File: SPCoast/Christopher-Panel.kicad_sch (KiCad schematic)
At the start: 23 parts, among them U10028 0x27, U10029 0x28, U10030 0x29

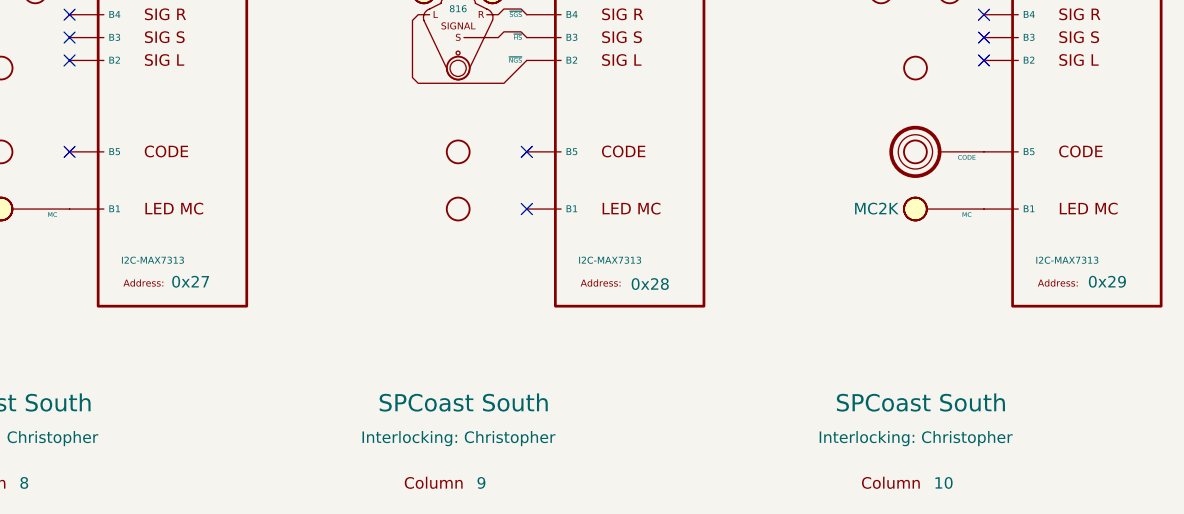
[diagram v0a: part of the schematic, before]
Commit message: chore(kicad): SPCoast symbols refreshed, field attribute visibility, no-connects on unused pins (owner's edit, baseline)
Owner, 2026-10-08: updated symbols from the libraries (the field pin direction flip, InterlockingPlant
61269e0), adjusted attribute visibility, added 22 no-connect markers on unused pins.

Verified (committed as saved, no edits):
- 485 components, 648 nets; every net identical to the previous commit.
- ERC 53 -> 20 messages (13 errors, 7 warnings). Remaining: unconnected HOUSE H / aux MC pins
  (Gilroy Caltrain, Luchessa, Watsonville); Corporal SW11901 still Railroad:Switch_HandThrow (not in
  the library) with open N/R legs; Sargent switch 1 open N/R legs; Christopher Panel U10029 A6 open
  while lamp LMP10093 carries a no-connect; 5 inherited wire stubs.
- Every instance path starts at the root uuid.

Co-Authored-By: Claude Opus 5.5 <noreply@anthropic.com>
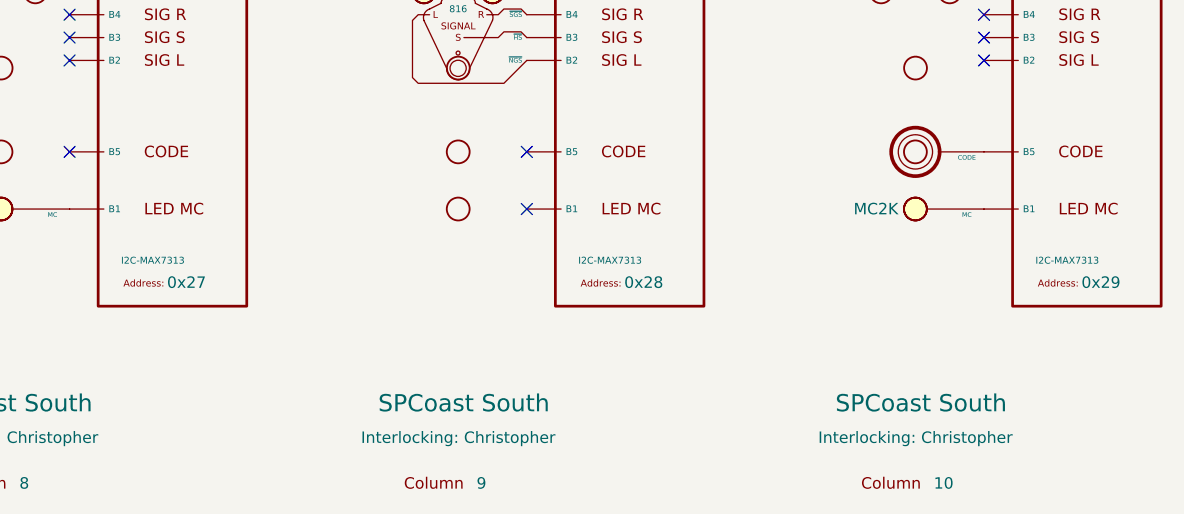
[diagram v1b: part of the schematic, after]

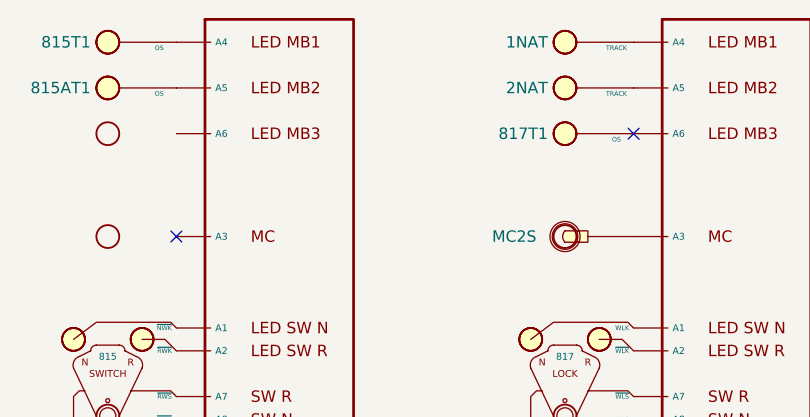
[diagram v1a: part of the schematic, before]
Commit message: fix(kicad): SPCoast ERC clean: Corporal SW11901 to Switch_Manual_Sensed, Christopher lamp fixed, no-connects (owner's edit, baseline)
Owner, 2026-10-08. Corporal and Sargent's industry tracks (the beet loader) join each other outside
CTC: dark track, no routes, no NextCP.

Verified (committed as saved, no edits): 485 components, 648 nets; ERC 0 errors, 0 warnings.

Co-Authored-By: Claude Opus 5.5 <noreply@anthropic.com>
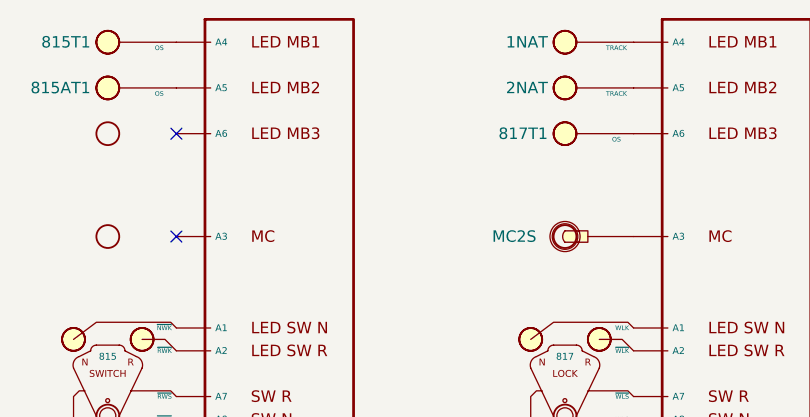
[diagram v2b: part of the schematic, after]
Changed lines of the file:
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@@
+	)
+	(no_connect
+		(at 138.43 36.83)
 	)
 	(no_connect
@@
 	)
 	(no_connect
-		(at 189.23 36.83)
-	)
-	(no_connect

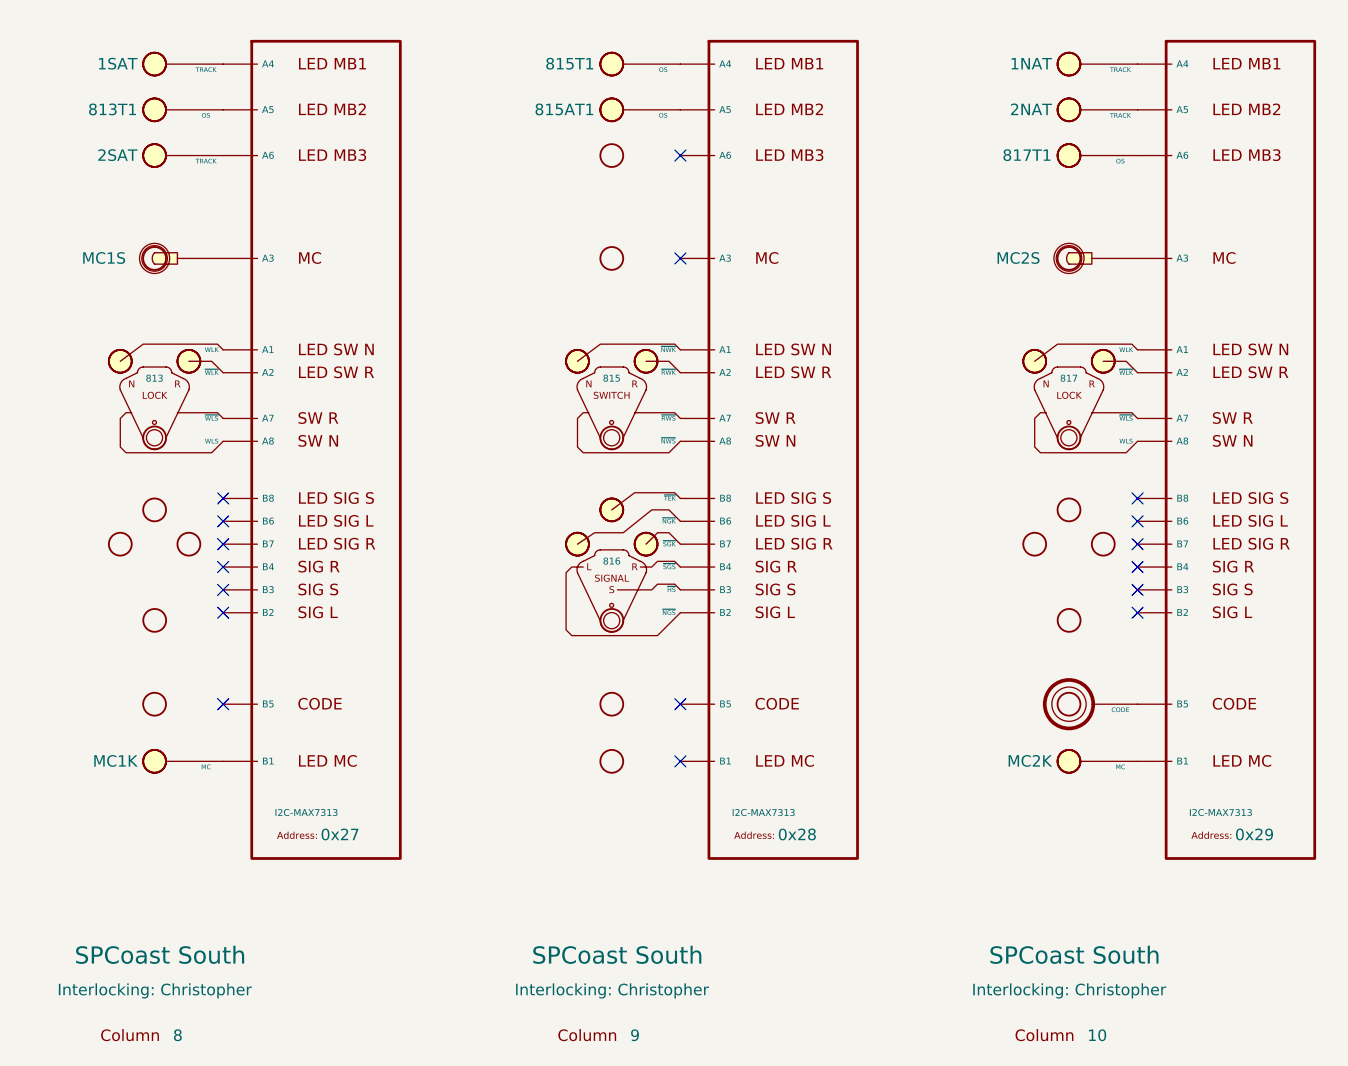
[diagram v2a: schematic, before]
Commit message: feat(spcoast): every sheet on the four Railroad libraries (checkpoint step 6, mechanical half)
By SPCoast/edits/2026-10-12-migrate-libraries.py, run once with KiCad closed: 483 instances
remapped across 16 sheets, embedded definitions replaced by the library blocks, instance fields
synced (Kind, ControlToken, Vital, NormalIs, Chain, Index dropped; Indications renamed
IndicationCeiling; Hold_ms renamed hold_ms; a pixel's Index became its Address; Rulebook kept
on the four Luchessa markers because the compiler still reads it), and 22 units added at the
same position for the plates and devices that are multi-unit now. Owner's choices: every plant
head CPL; Sargent's semaphore UQ; the 0x27 PCA9685 as PWM; the office MAX7313s as the
SPCoastcTc variant. Left by hand: the two AUXILIARY_TRAFFIC markers on Watsonville (retired).

Verified (production/migration-gate.txt, netlist_diff.py against pre-migration.net): office
and local plates and all chips keep their connectivity; 14 nets lost, all on Sargent, where
the six field devices (DevSW13001, 13004 to 13007, 13012) have new pin positions and must be
re-wired by hand. ERC: lib_symbol_issues 492 before (unregistered libraries) to 2 after (the
retired markers); the 29 unconnected pins are those devices and their chip pins.

Co-Authored-By: Claude Fable 5.1 <noreply@anthropic.com>
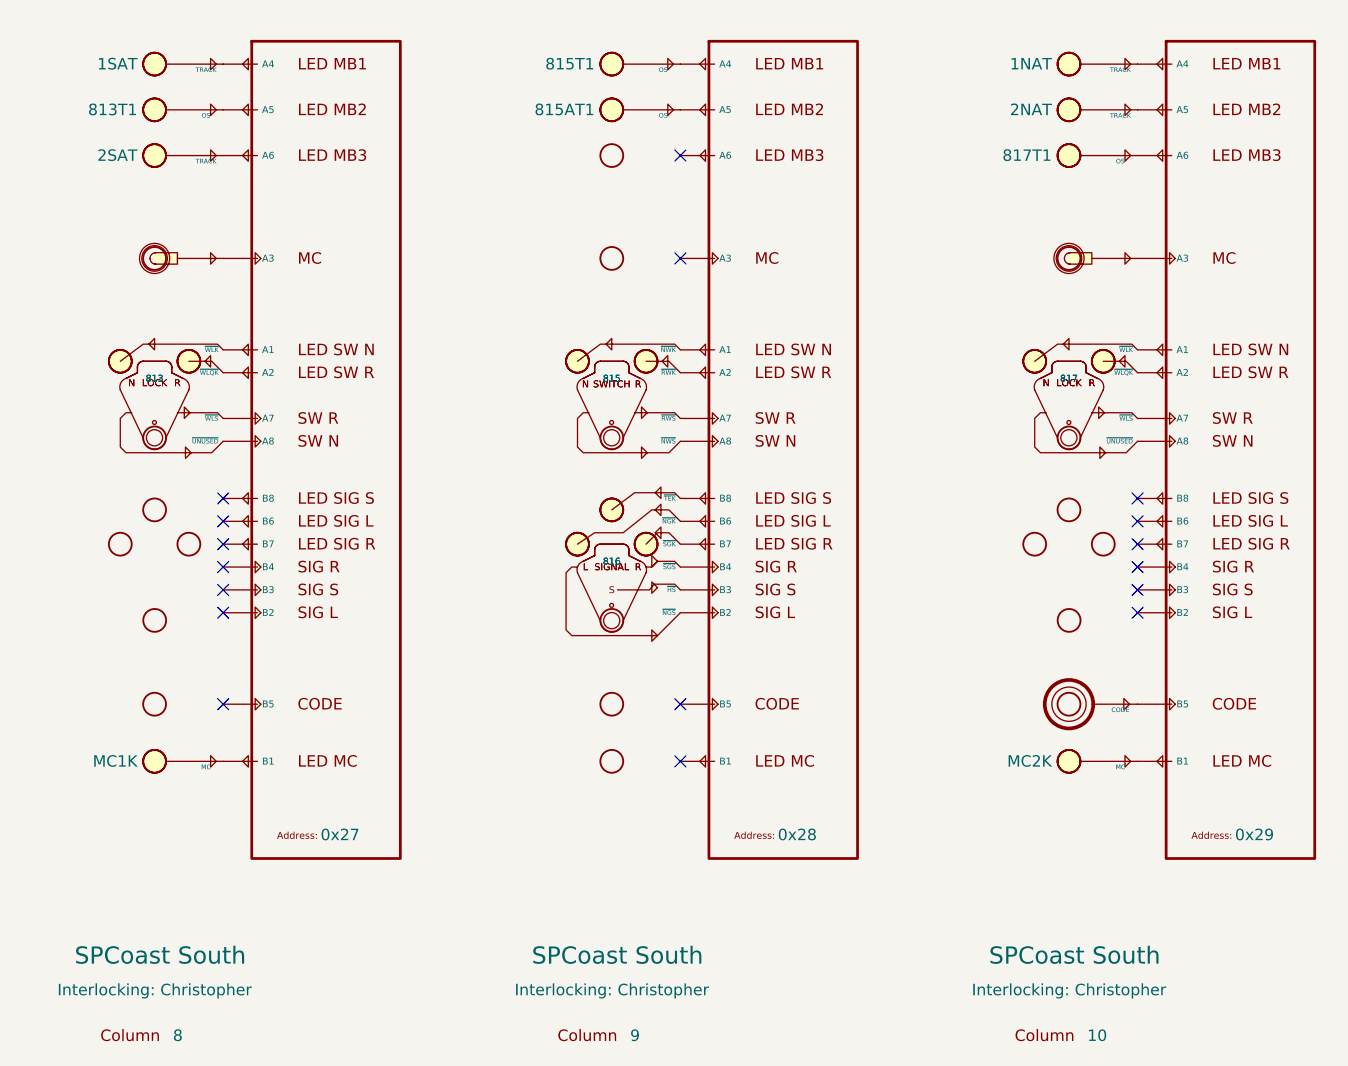
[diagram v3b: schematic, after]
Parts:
- added unit 2 of LKL10008
- added unit 2 of LKL10010
- added unit 2 of SGL10009
- added unit 2 of SWL10009
- CDE10010: symbol RailroadPanel:PanelCode -> Railroad-Office:PanelCode; Appliance (none) -> lever; Kind CODE -> (none); Pin.CODE (none) -> binary; Style (none) -> code
- COL10028, COL10029, COL10030: symbol RailroadPanel:PanelColumn -> Railroad-Office:PanelColumn
- LKL10008, LKL10010: symbol RailroadPanel:PanelLock -> Railroad-Office:PanelLock; Appliance (none) -> lever; Invert (none) -> WLK; Kind LOCK_LEVER_2LAMP_2CONTACT -> (none); Pin.UNUSED (none) -> binary; Pin.WLK (none) -> binary; Pin.WLQK (none) -> binary; Pin.WLS (none) -> binary; Style (none) -> lock
- LMP10081, LMP10083, LMP10101, LMP10102, MCK10008, MCK10010: symbol RailroadPanel:PanelLamp-YELLOW -> Railroad-Office:PanelLamp-YELLOW; Appliance (none) -> lamp; Kind LAMP -> (none); Pin.LAMP (none) -> binary; Style (none) -> indication
- LMP10082, LMP10091, LMP10092, LMP10093: symbol RailroadPanel:PanelLamp-RED -> Railroad-Office:PanelLamp-RED; Appliance (none) -> lamp; Kind LAMP -> (none); Pin.LAMP (none) -> binary; Style (none) -> indication
- MCL10008: symbol RailroadPanel:PanelMCall -> Railroad-Office:PanelMCall; Appliance (none) -> lever; ControlToken MC1S -> (none); Kind MAINTAINER_CALL -> (none); Pin.S (none) -> binary; Style (none) -> maintainer_call; Vital NO -> (none)
- MCL10010: symbol RailroadPanel:PanelMCall -> Railroad-Office:PanelMCall; Appliance (none) -> lever; ControlToken MC2S -> (none); Kind MAINTAINER_CALL -> (none); Pin.S (none) -> binary; Style (none) -> maintainer_call; Vital NO -> (none)
- SGL10009: symbol RailroadPanel:PanelSignal -> Railroad-Office:PanelSignal; Appliance (none) -> lever; Kind SIGNAL_LEVER -> (none); Pin.HS (none) -> binary; Pin.NGK (none) -> binary; Pin.NGS (none) -> binary; Pin.SGK (none) -> binary; Pin.SGS (none) -> binary; Pin.TEK (none) -> binary; Style (none) -> signal
- SWL10009: symbol RailroadPanel:PanelSwitch -> Railroad-Office:PanelSwitch; Appliance (none) -> lever; Kind SWITCH_LEVER -> (none); Pin.NWK (none) -> binary; Pin.NWS (none) -> binary; Pin.RWK (none) -> binary; Pin.RWS (none) -> binary; Style (none) -> switch
- U10028, U10029, U10030: symbol RailroadPanel:Driver-I2C-MAX7313 -> Railroad-HardwareIO:Driver-I2C-MAX7313-SPCoastcTc; IC (none) -> MAX7313; Kind I2C-MAX7313 -> (none); Pin.A1 (none) -> binary; Pin.A2 (none) -> binary; Pin.A3 (none) -> binary; Pin.A4 (none) -> binary; Pin.A5 (none) -> binary; Pin.A6 (none) -> binary; Pin.A7 (none) -> binary; Pin.A8 (none) -> binary; Pin.B1 (none) -> binary; Pin.B2 (none) -> binary; Pin.B3 (none) -> binary; Pin.B4 (none) -> binary; Pin.B5 (none) -> binary; Pin.B6 (none) -> binary; Pin.B7 (none) -> binary; Pin.B8 (none) -> binary
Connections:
- net at U10029.15 (B7): now also SGL10009.5 (~{SGK}); no longer SGL10009.5 (~{SGK})
- net at U10029.14 (B6): now also SGL10009.6 (~{NGK}); no longer SGL10009.6 (~{NGK})
- net at U10029.16 (B8): now also SGL10009.7 (~{TEK}); no longer SGL10009.7 (~{TEK})
- net at U10029.1 (A1): now also SWL10009.5 (~{NWK}); no longer SWL10009.5 (~{NWK})
- net at U10029.2 (A2): now also SWL10009.4 (~{RWK}); no longer SWL10009.4 (~{RWK})
- net at U10030.1 (A1): now also LKL10010.5 (~{WLK}); no longer LKL10010.5 (WLK)
- net at U10030.2 (A2): now also LKL10010.4 (~{WLQK}); no longer LKL10010.4 (~{WLK})
- net at U10028.2 (A2): now also LKL10008.4 (~{WLQK}); no longer LKL10008.4 (~{WLK})
- net at U10028.1 (A1): now also LKL10008.5 (~{WLK}); no longer LKL10008.5 (WLK)

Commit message: chore: owner's Sargent cleanup and library edits of 2026-10-12 and 13 (baseline)
Co-Authored-By: Claude Fable 5.1 <noreply@anthropic.com>
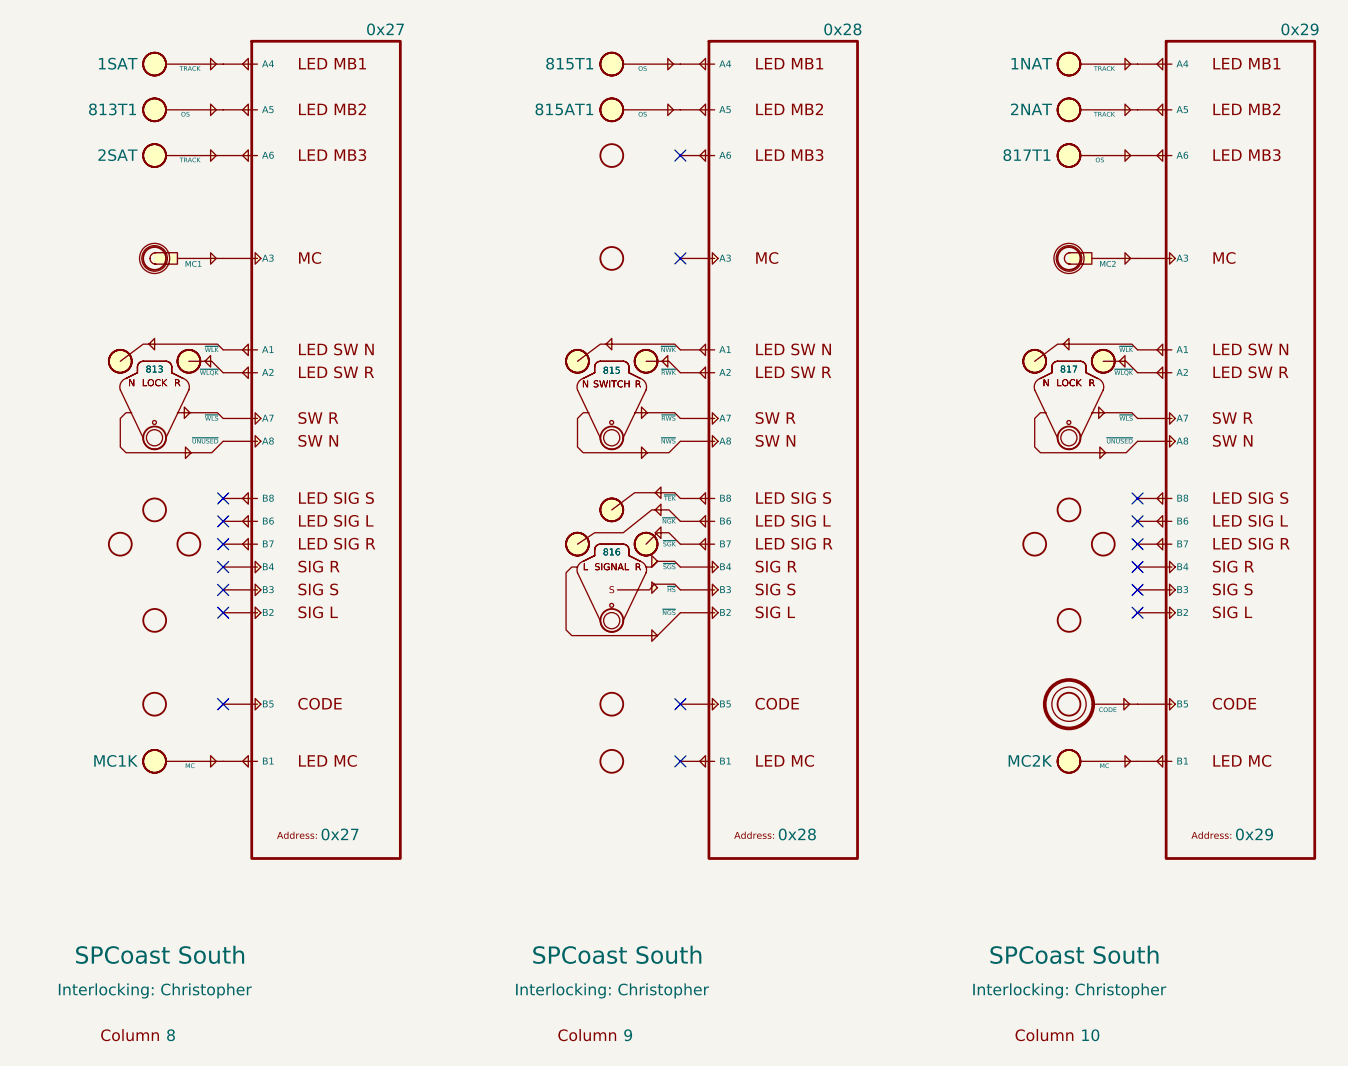
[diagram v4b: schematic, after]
